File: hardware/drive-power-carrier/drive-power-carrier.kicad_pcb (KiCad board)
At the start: 2 copper layers, 30 x 18 mm, 25 parts, among them U1 TA6586 DIP8, U2 TPS73701DRBR, U3 MAX40200AUK+T

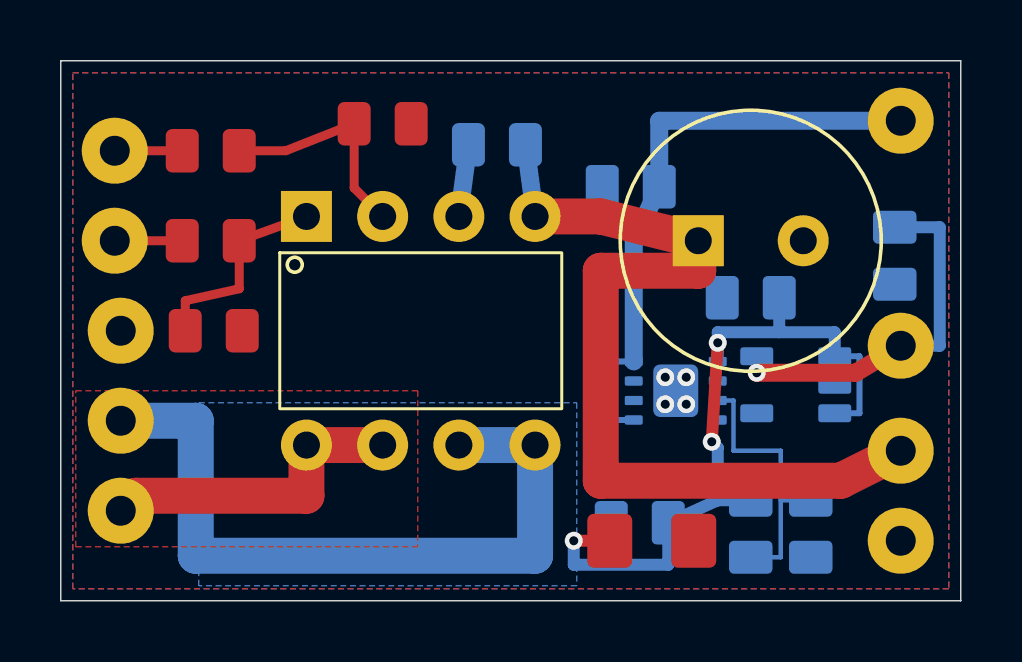
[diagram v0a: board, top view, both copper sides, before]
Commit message: Correct MAX40200 footprint and clearance reserve from reviewed manufacturer drawings
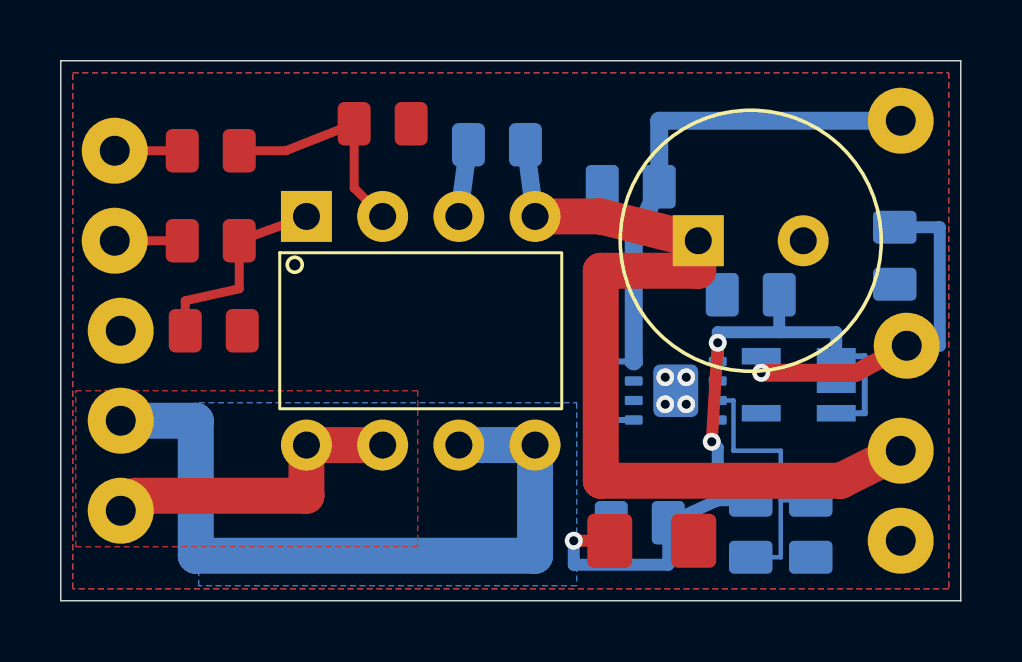
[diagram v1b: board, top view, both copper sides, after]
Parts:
- U3: footprint RaceRemote_DrivePower:SOT23_5_Provisional_U3 -> RaceRemote_DrivePower:SOT23_5_ADI_90_0174_B_U3
- moved H9 0.20 mm to (128.2, 109.5)
- moved C5 0.10 mm to (123.0, 107.8)
- moved U3 0.10 mm to (124.6, 110.8)

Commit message: Add dedicated XIAO ground landing and free traction input return
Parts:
- added H10: DRIVE_GND, RaceRemote_DrivePower:WirePad_1mm_H10, F.Cu at (118.0, 101.7)
